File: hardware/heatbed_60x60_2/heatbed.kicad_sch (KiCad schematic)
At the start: 1 part, among them J1 PWR

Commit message: Add a control board
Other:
- title: Reflow Plate Heatbed 60x60 mm -> Reflow Hot-Plate Heatbed 60x60 mm
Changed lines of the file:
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@@
   (paper "A4")
   (title_block
-    (title "Reflow Plate Heatbed 60x60 mm")
+    (title "Reflow Hot-Plate Heatbed 60x60 mm")
     (date "2023-03-19")
-    (rev "v1.0.0")
+    (rev "1.0.0")
     (company "I. Kajdan")
   )

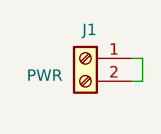
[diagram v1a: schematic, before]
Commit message: Increase holes' diameters
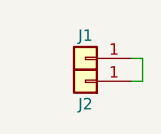
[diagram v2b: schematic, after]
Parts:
- removed J1: PWR, Connector_PinHeader_2.54mm:PinHeader_1x02_P2.54mm_Vertical, symbol Connector:Screw_Terminal_01x02
- added J1, J2: Conn_01x01, Connector_Pin:Pin_D1.3mm_L11.0mm, symbol Connector_Generic:Conn_01x01
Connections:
- new net: J1.1 (Pin_1), J2.1 (Pin_1)
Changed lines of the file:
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@@
     (stroke (width 0) (type default))
   )
-  (symbol (lib_id "Connector:Screw_Terminal_01x02") (at 147.32 100.33 0) (mirror y) (unit 1)
-    (in_bom yes) (on_board yes) (dnp no)
-    (property "Reference" "J1" (at 148.59 97.155 0)
-      (effects (font (size 1.27 1.27)) (justify left))
+  (symbol (lib_id "Connector_Generic:Conn_01x01") (at 147.32 100.33 180) (unit 1)
+    (in_bom yes) (on_board yes) (dnp no) (fields_autoplaced)
+    (property "Reference" "J1" (at 147.32 97.79 0)
+      (effects (font (size 1.27 1.27)))
     )
-    (property "Value" "PWR" (at 144.78 102.235 0)
-      (effects (font (size 1.27 1.27)) (justify left))
+    (property "Value" "Conn_01x01" (at 147.32 97.79 0)
+      (effects (font (size 1.27 1.27)) hide)
     )
-    (property "Footprint" "Connector_PinHeader_2.54mm:PinHeader_1x02_P2.54mm_Vertical" (at 147.32 100.33 0)
+    (property "Footprint" "Connector_Pin:Pin_D1.3mm_L11.0mm" (at 147.32 100.33 0)
       (effects (font (size 1.27 1.27)) hide)
     )
@@
     )
     (pin "1")
-    (pin "2")
     (instances
       (project "heatbed"
@@
         )
       )
+    )
+  )
+  (symbol (lib_id "Connector_Generic:Conn_01x01") (at 147.32 102.87 180) (unit 1)
+    (in_bom yes) (on_board yes) (dnp no)
+    (property "Reference" "J2" (at 147.32 105.41 0)
+      (effects (font (size 1.27 1.27)))
+    )
+    (property "Value" "Conn_01x01" (at 147.32 100.33 0)
+      (effects (font (size 1.27 1.27)) hide)
+    )
+    (property "Footprint" "Connector_Pin:Pin_D1.3mm_L11.0mm" (at 147.32 102.87 0)
+      (effects (font (size 1.27 1.27)) hide)
+    )
+    (property "Datasheet" "~" (at 147.32 102.87 0)
+      (effects (font (size 1.27 1.27)) hide)
+    )
+    (pin "1")
+    (instances
+      (project "heatbed"
+        (path "/f6f1e229-f102-463e-b32b-76ca65db5faf"
+          (reference "J2") (unit 1)
+        )
+      )
